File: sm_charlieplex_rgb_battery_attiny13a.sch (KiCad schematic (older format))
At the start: 12 parts, among them SW1 SW_Push, U1 ATtiny10-TS

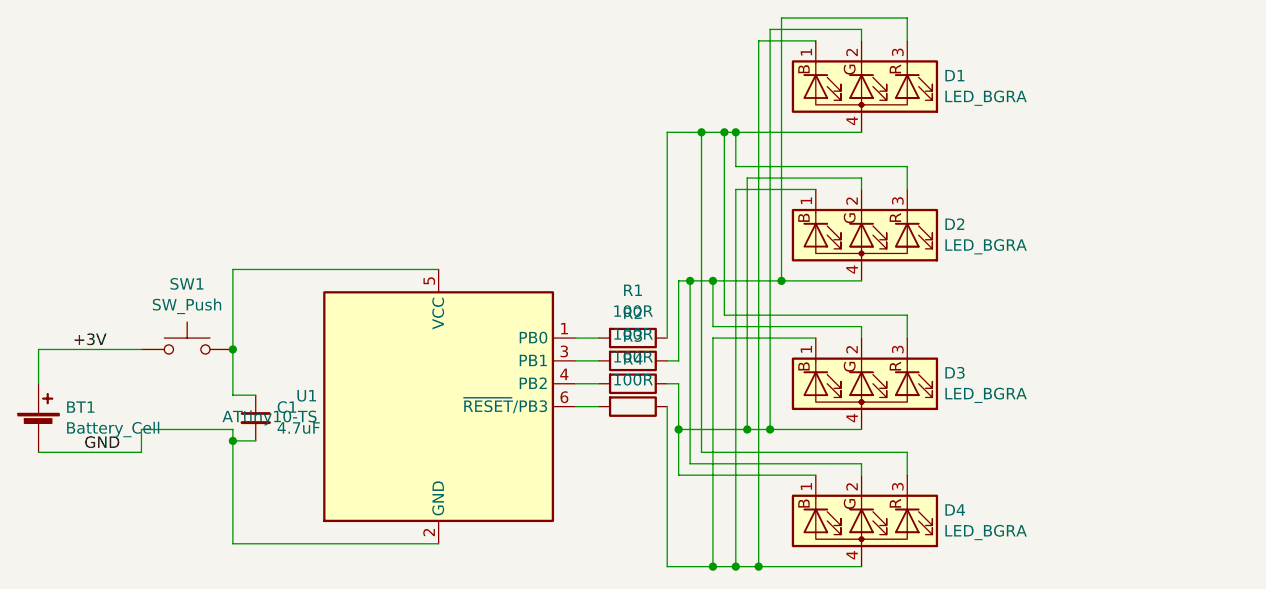
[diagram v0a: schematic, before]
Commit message: Reformat for attiny13
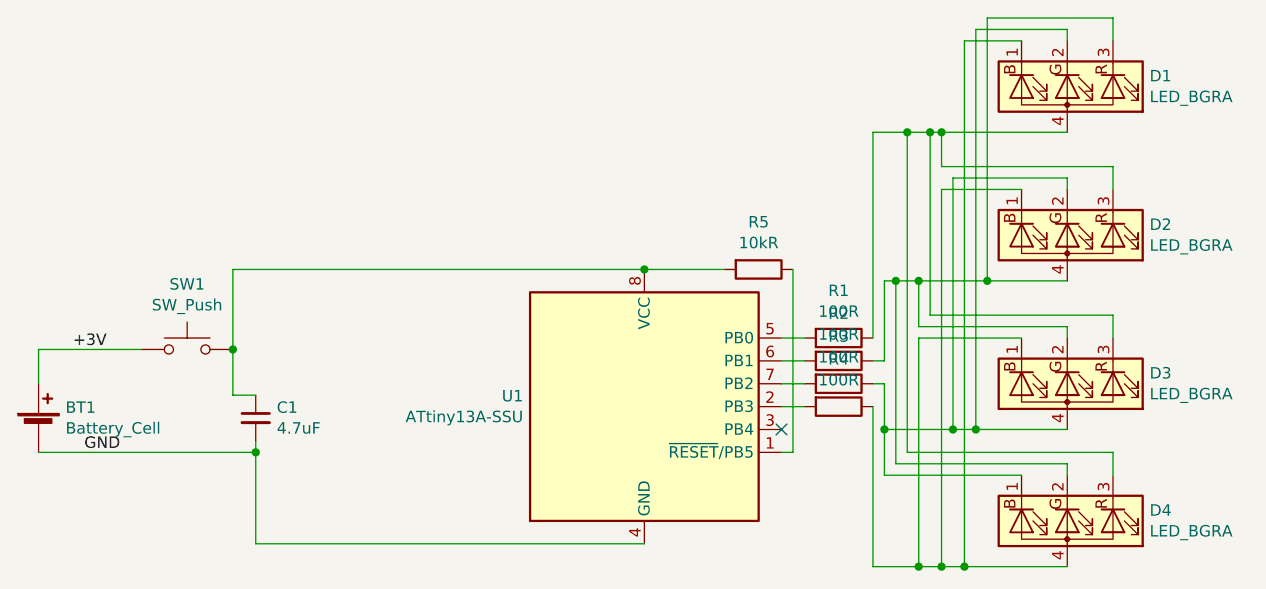
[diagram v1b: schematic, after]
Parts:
- removed U1: ATtiny10-TS, Package_TO_SOT_SMD:SOT-23-6, symbol MCU_Microchip_ATtiny:ATtiny10-TS
- added R5: 10kR, Resistor_SMD:R_0805_2012Metric, symbol Device:R
- added U1: ATtiny13A-SSU, Package_SO:SOIC-8_3.9x4.9mm_P1.27mm, symbol MCU_Microchip_ATtiny:ATtiny13A-SSU
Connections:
- net GND: now also U1.4 (GND)
- net at R1.2: now also U1.5 (PB0)
- net at R2.2: now also U1.6 (PB1)
- net at R3.2: now also U1.7 (PB2)
- net at C1.1, SW1.2: now also R5.2, U1.8 (VCC)
- net at R4.2: now also U1.2 (PB3)
- new net: R5.1, U1.1 (~RESET~/PB5)
- no-connect marks 0 -> 1
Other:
- moved on the sheet: D1, D2, D3, D4, R1, R2, R3, R4
